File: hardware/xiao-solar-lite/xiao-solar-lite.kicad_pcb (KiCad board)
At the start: 2 copper layers, 30.5 x 28.5 mm, 36 parts, among them J1 SOLAR, J3 OUT (to Xiao 5V), J4 BATTERY, J5 I2C + CE, Q2 AO3400A (ship FET), U1 BQ25798RQMR

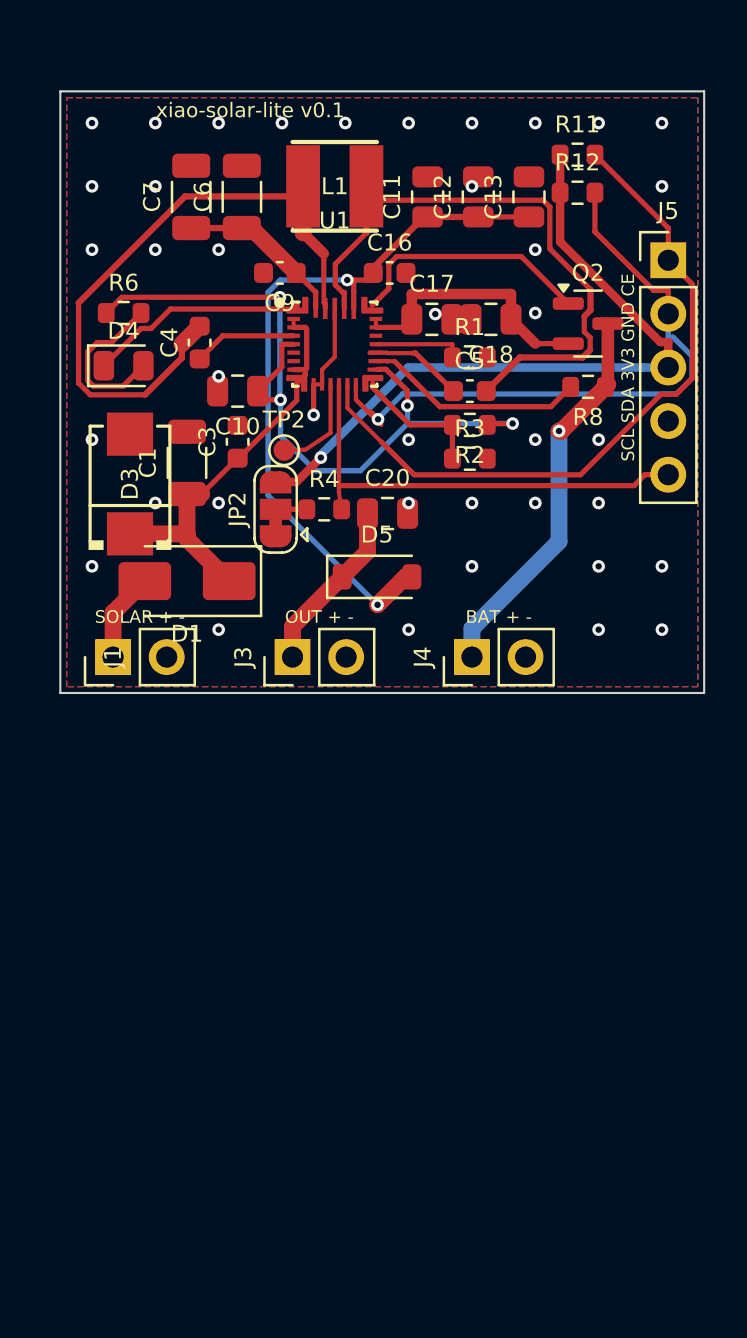
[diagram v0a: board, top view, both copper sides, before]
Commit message: hardware: xiao-solar-lite v0.2 as third layer under XIAO + Wio
The module now stacks under the standard XIAO nRF52840 + Wio-SX1262
sandwich through the 14 XIAO holes: CE on D0, SCL/SDA on D6/D7, 3V3,
GND, and SYS through B5819W to the 5V pin. 23 x 53 mm, charger below the
stack, only flat parts under it. Separate 4-pin I2C header for sensors.
Keepouts keep signal tracks off the L1 switch node and off the edge.

Co-Authored-By: Claude Opus 5.5 <noreply@anthropic.com>
Claude-Session: https://claude.ai/code/session_01P5Km81NY9NPL6RpKFGVEbH
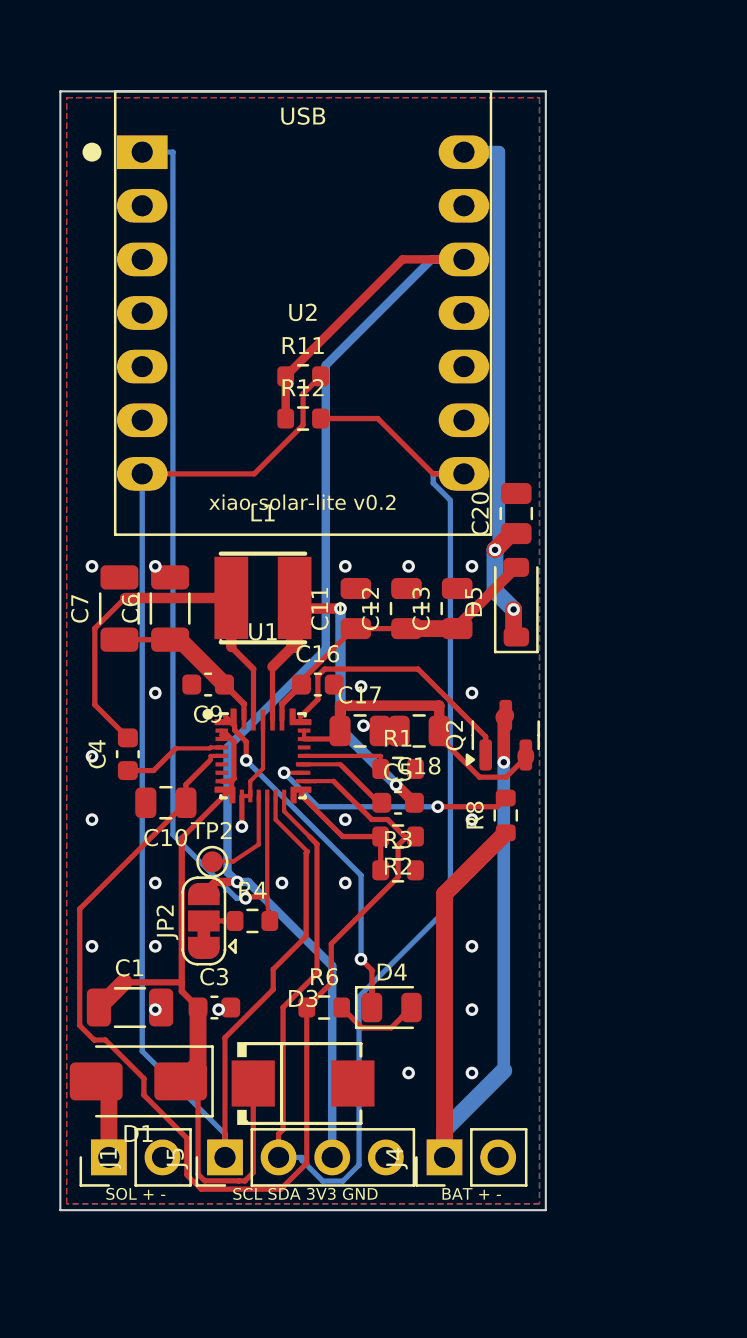
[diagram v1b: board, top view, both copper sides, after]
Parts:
- removed J3: OUT (to Xiao 5V), Connector_PinHeader_2.54mm:PinHeader_1x02_P2.54mm_Vertical
- added U2: XIAO + Wio stack, xiao_solar:XIAO_14P_2.54_21x17.8mm, F.Cu at (111.5, 110.5)
- J5: value I2C + CE -> I2C sensors; footprint Connector_PinHeader_2.54mm:PinHeader_1x05_P2.54mm_Vertical -> Connector_PinHeader_2.54mm:PinHeader_1x04_P2.54mm_Vertical
- moved J5 47.4 mm to (107.8, 150.5), turned to 90 degrees
- moved R6 34.2 mm to (112.5, 143.4)
- moved D4 32.9 mm to (115.7, 143.4)
- moved D3 29.6 mm to (111.5, 147.0), turned to 0 degrees
- moved C3 26.8 mm to (107.3, 143.4), turned to 0 degrees
- moved C1 25.9 mm to (103.3, 143.4), turned to 0 degrees
- moved D1 23.8 mm to (103.7, 146.9)
- moved J4 23.7 mm to (118.2, 150.5)
- moved J1 23.7 mm to (102.3, 150.5)
- moved R8 20.7 mm to (121.1, 134.3), turned to 90 degrees
- moved Q2 19.9 mm to (121.1, 130.5), turned to 90 degrees
- moved C17 19.8 mm to (114.2, 130.3)
- moved C18 19.8 mm to (117.0, 130.3)
- moved JP2 19.8 mm to (106.8, 139.3)
- moved R2 19.8 mm to (116.0, 135.3)
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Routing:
- net SDA: track 31.6 -> 67.4 mm, vias 1 -> 0
- net 3V3: track 33.3 -> 65.0 mm
- net SCL: track 33.2 -> 64.6 mm
- net BATT+: track 18.5 -> 38.8 mm
- net SYS: track 34.5 -> 14.7 mm, vias 2 -> 0
- net REGN: track 37.0 -> 55.7 mm, vias 4 -> 0
- net CE: track 26.9 -> 45.5 mm, vias 0 -> 1
- net VOUT: track 8.27 -> 26.4 mm, vias 0 -> 2
- net VBUS: track 19.9 -> 36.1 mm
- net SW1: track 30.4 -> 19.1 mm
- net SW2: track 29.1 -> 19.1 mm, vias 0 -> 2
- net STAT: track 10.4 -> 17.5 mm, vias 0 -> 2
- net LED_STAT: track 7.79 -> 4.79 mm
- net BAT: track 12.8 -> 15.3 mm
- net BATP: track 10.5 -> 12.3 mm, vias 0 -> 2
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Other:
- board size 30.5 x 28.5 mm -> 23 x 53 mm
- board text added: "SCL SDA 3V3 GND"
- board text added: "SOL + -"
- board text added: "xiao-solar-lite v0.2"
- board text removed: "OUT + -"
- board text removed: "SCL SDA 3V3 GND CE"
- board text removed: "SOLAR + -"
- board text removed: "xiao-solar-lite v0.1"

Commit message: hardware: charger zone per BQ25798 layout guide, v0.3 of both boards
- tools/charger.py: shared BQ25798 cluster (placement, PMID/SYS/VBUS/BAT/SW
  copper zones, hand routes) for xiao-solar and xiao-solar-lite
- 100 nF PMID/SYS caps at the pins, SW short and wide to L1, BTST/REGN/GND
  through vias under the package, BAT halves joined on B.Cu
- lite: TI cap counts (VBUS 2, PMID 3, SYS 5), 23 x 57 mm, D5 fed from SYS
- thermal spokes on small parts, solid on charger power caps
- routing: zone copper goes to Freerouting as fixed hatched wires, locked
  hand routes survive the finish pass; JLC CPL rotation fix for SOT-23/LED
- both boards 0 unconnected; READMEs, Gerber, BOM, CPL, PDFs, images

Co-Authored-By: Claude Opus 5.5 <noreply@anthropic.com>
Claude-Session: https://claude.ai/code/session_01P5Km81NY9NPL6RpKFGVEbH
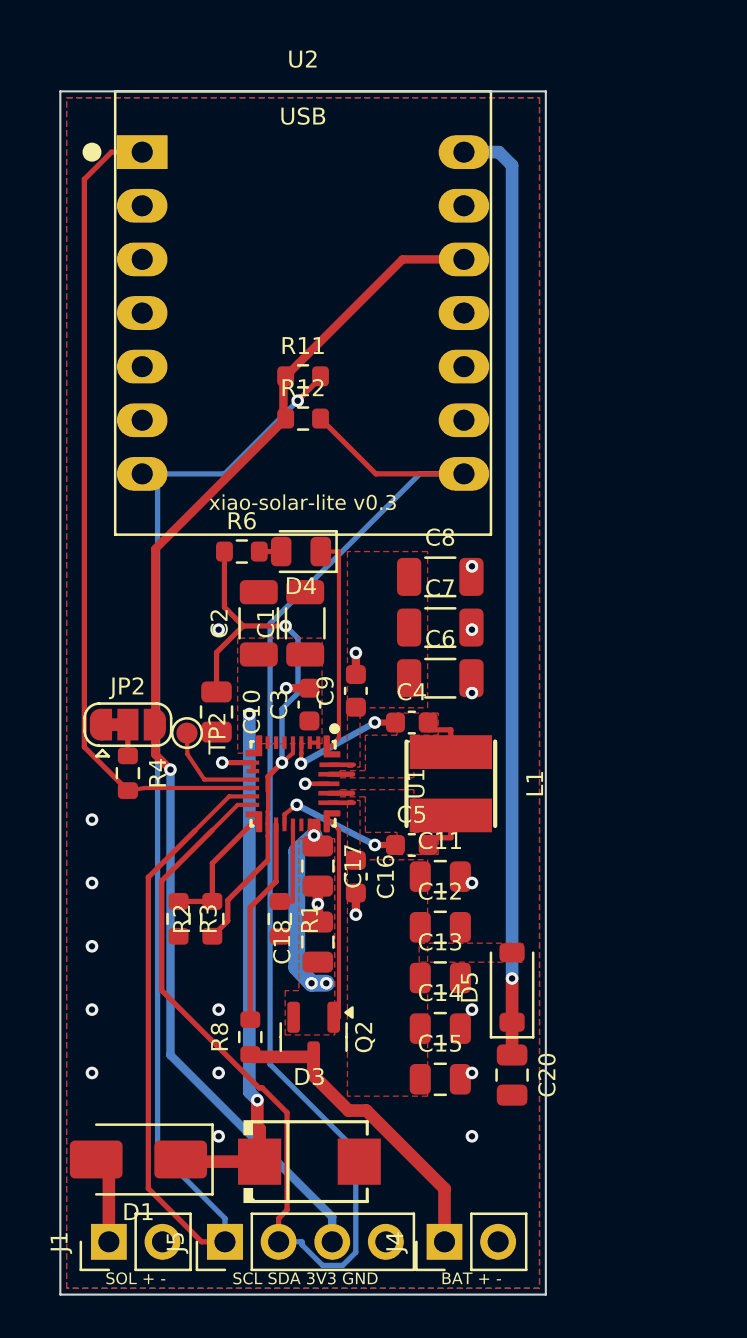
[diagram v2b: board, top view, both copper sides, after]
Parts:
- added C14: 10u/25V, Capacitor_SMD:C_0805_2012Metric, F.Cu at (118.0, 144.4)
- added C15: 10u/25V, Capacitor_SMD:C_0805_2012Metric, F.Cu at (118.0, 146.8)
- added C2: 10u/50V, Capacitor_SMD:C_1206_3216Metric, F.Cu at (109.4, 125.2)
- added C8: 10u/50V, Capacitor_SMD:C_1206_3216Metric, F.Cu at (118.0, 123.0)
- moved C20 26.6 mm to (121.4, 146.6), turned to -90 degrees
- moved D4 22.0 mm to (111.4, 121.8), turned to 180 degrees
- moved R6 21.9 mm to (108.6, 121.8)
- moved C1 20.0 mm to (111.6, 125.2), turned to 90 degrees
- moved D5 18.3 mm to (121.4, 142.4)
- moved C13 17.5 mm to (118.0, 142.0), turned to 0 degrees
- moved Q2 16.9 mm to (112.0, 144.8), turned to -90 degrees
- moved R8 16.0 mm to (109.0, 144.8)
- moved C7 15.2 mm to (118.0, 125.4), turned to 0 degrees
- moved C12 15.2 mm to (118.0, 139.6), turned to 0 degrees
- moved C3 15.0 mm to (111.8, 129.1), turned to 90 degrees
- moved C4 13.5 mm to (116.7, 129.9), turned to 0 degrees
- moved C11 13.3 mm to (118.0, 137.2), turned to 0 degrees
- moved C6 13.2 mm to (118.0, 127.8), turned to 0 degrees
- moved L1 12.5 mm to (118.5, 132.8), turned to -90 degrees
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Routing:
- net REGN: track 55.7 -> 27.4 mm, vias 0 -> 2
- net BATT+: track 38.8 -> 15.3 mm, vias 1 -> 0
- net VOUT: track 26.4 -> 44.7 mm, vias 2 -> 1
- net SW1: track 19.1 -> 3.62 mm
- net SW2: track 19.1 -> 3.62 mm, vias 2 -> 0
- net SDA: track 67.4 -> 81.5 mm
- net SYS: track 14.7 -> 1.18 mm
- net VBUS: track 36.1 -> 25.6 mm, vias 0 -> 2
- net SCL: track 64.6 -> 74.1 mm, vias 0 -> 1
- net STAT: track 17.5 -> 10.2 mm, vias 2 -> 0
- net 3V3: track 65.0 -> 57.9 mm
- net PMID: track 7.89 -> 1.15 mm
- net CE: track 45.5 -> 39.0 mm, vias 1 -> 0
- net BAT: track 15.3 -> 9.74 mm, vias 0 -> 3
- net LED_STAT: track 4.79 -> 1.04 mm
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- added copper zone on F.Cu, net BAT
- added copper zone on F.Cu, net PMID
- added copper zone on F.Cu, net SW1
- added copper zone on F.Cu, net SW2
- added copper zone on F.Cu, net SYS
- added copper zone on F.Cu, net VBUS
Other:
- board size 23 x 53 mm -> 23 x 57 mm
- board text added: "xiao-solar-lite v0.3"
- board text removed: "xiao-solar-lite v0.2"

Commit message: hardware: two vias per power layer change, no vias in pads
- BAT halves joined on B.Cu with two vias at each end (C17/C18/Q2 moved)
- refill.py: second via next to every power-net via that is alone
- lite: VBUS from the input diodes as one 0.8 mm B.Cu run, two vias at
  each end; main: fixed landing vias for the VBUS bus in the VBUS copper
- stitching/island vias stay off pads (kicad-happy VP-001 findings)
- main: own GND via for C22 between the module rows
- Gerber, BOM, CPL, PDFs and images regenerated; both boards 0 unconnected

Co-Authored-By: Claude Opus 5.5 <noreply@anthropic.com>
Claude-Session: https://claude.ai/code/session_01P5Km81NY9NPL6RpKFGVEbH
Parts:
- moved C17 1.60 mm to (112.2, 138.3)
- moved C18 1.60 mm to (112.2, 141.9)
- moved Q2 1.60 mm to (112.0, 146.4)
- moved R8 1.60 mm to (109.0, 146.4)
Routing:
- net SCL: track 74.1 -> 51.5 mm, vias 1 -> 2
- net VBUS: track 25.6 -> 35.9 mm, vias 2 -> 6
- net SDA: track 81.5 -> 76.1 mm
- net 3V3: track 57.9 -> 63.4 mm
- net REGN: track 27.4 -> 23.2 mm
- net BAT: track 9.74 -> 12.6 mm, vias 3 -> 4
- net VOUT: track 44.7 -> 46.7 mm, vias 1 -> 2
- net BATT+: track 15.3 -> 13.7 mm
- net SDRV: track 9.65 -> 11.2 mm
- net BATP: track 9.76 -> 11.4 mm
- net GND: vias 22 -> 12

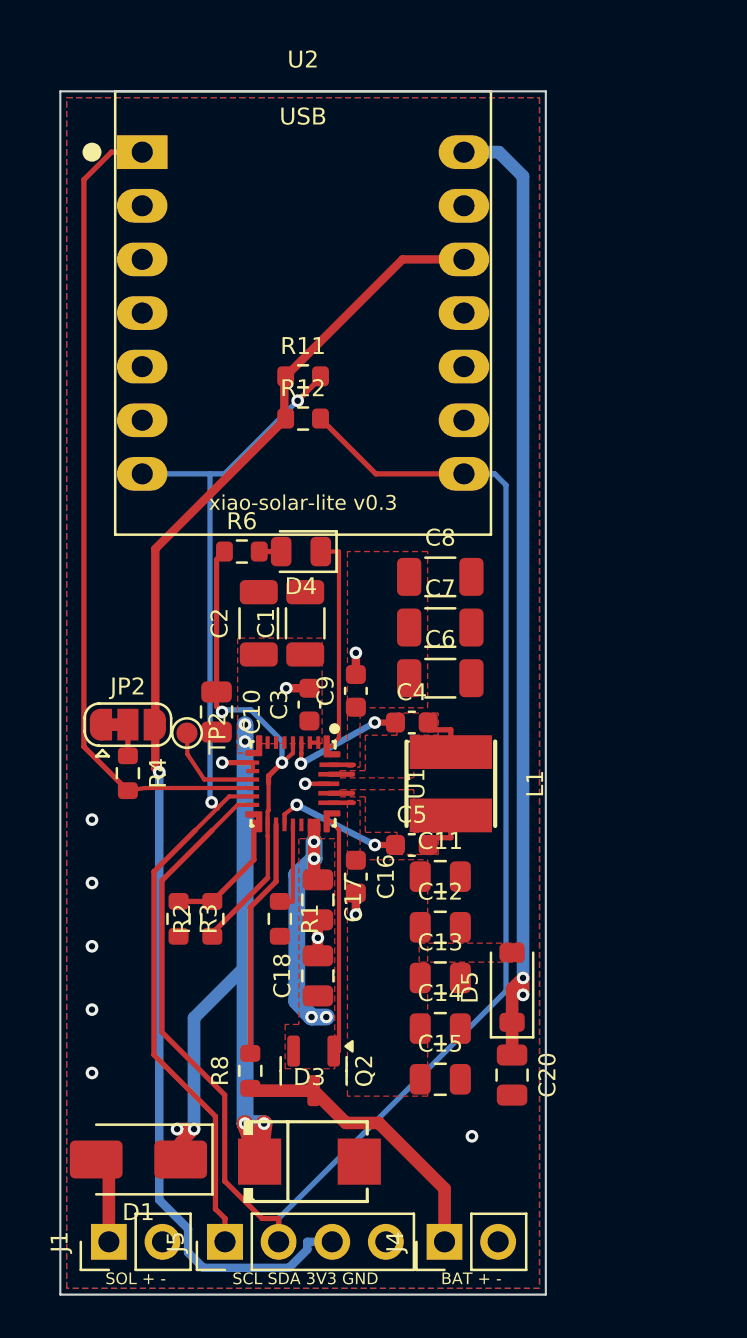
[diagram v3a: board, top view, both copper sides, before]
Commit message: hardware: xiao-solar v0.4 (no loads, INA219, 48x71.5) + block schematics for both boards
Co-Authored-By: Claude Opus 5.5 <noreply@anthropic.com>
Claude-Session: https://claude.ai/code/session_01P5Km81NY9NPL6RpKFGVEbH
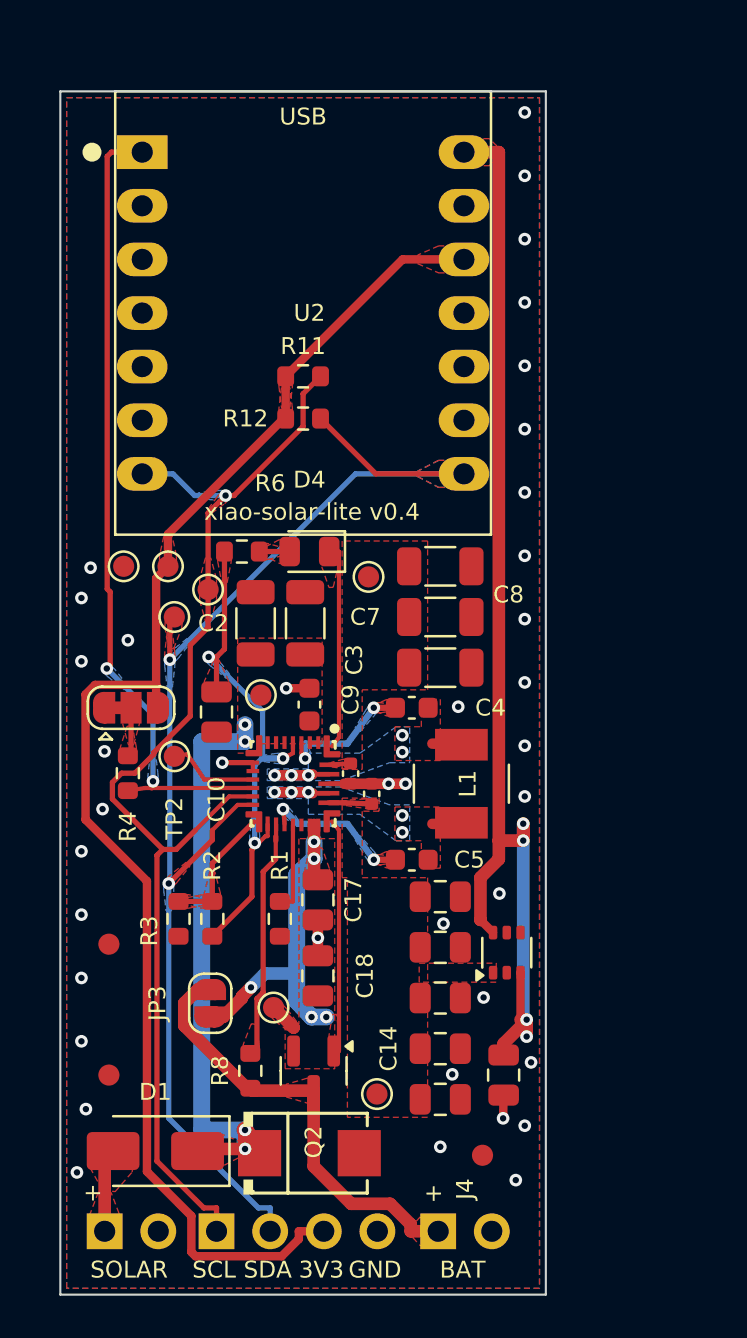
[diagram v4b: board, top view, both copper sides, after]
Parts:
- added FID1: Fiducial, Fiducial_1mm_Mask2mm, F.Cu at (102.3, 140.4)
- added FID2: Fiducial, Fiducial_1mm_Mask2mm, F.Cu at (120.0, 150.4)
- added FID3: Fiducial, Fiducial_1mm_Mask2mm, F.Cu at (102.3, 146.6)
- added JP3: no ship FET (LiFePO4), Jumper:SolderJumper-2_P1.3mm_Open_RoundedPad1.0x1.5mm, F.Cu at (107.1, 143.2)
- added TP10: SDA, TestPoint:TestPoint_Pad_D1.0mm, F.Cu at (105.4, 124.9)
- added TP3: VBUS, TestPoint:TestPoint_Pad_D1.0mm, F.Cu at (109.5, 128.6)
- added TP4: PMID, TestPoint:TestPoint_Pad_D1.0mm, F.Cu at (114.6, 123.0)
- added TP5: SYS, TestPoint:TestPoint_Pad_D1.0mm, F.Cu at (115.0, 147.5)
- added TP6: BAT, TestPoint:TestPoint_Pad_D1.0mm, F.Cu at (110.1, 143.4)
- added TP7: GND, TestPoint:TestPoint_Pad_D1.0mm, F.Cu at (103.0, 122.5)
- added TP8: 3V3, TestPoint:TestPoint_Pad_D1.0mm, F.Cu at (105.1, 122.5)
- added TP9: SCL, TestPoint:TestPoint_Pad_D1.0mm, F.Cu at (107.0, 123.6)
- C16: footprint Capacitor_SMD:C_0603_1608Metric -> Capacitor_SMD:C_0402_1005Metric
- C9: value 100n -> 100n/50V; footprint Capacitor_SMD:C_0603_1608Metric -> Capacitor_SMD:C_0402_1005Metric
- D1: value SS34 -> SS54
- D5: value B5819W -> LM66100; footprint Diode_SMD:D_SOD-123 -> Package_TO_SOT_SMD:SOT-363_SC-70-6
- L1: value 2.2uH 3.2A -> 2.2uH 4A molded (MWSA0402S); footprint xiao_solar:IND-SMD_L4.0-W4.0_FNR40XXS -> xiao_solar:IND-SMD_L4.4-W4.2_MWSA0402S
- moved C16 3.99 mm to (114.8, 133.3), turned to 90 degrees
- moved C9 3.93 mm to (113.8, 132.3), turned to -90 degrees
- moved D5 1.67 mm to (121.2, 140.8)
- moved TP2 1.25 mm to (105.4, 131.5)
- moved C11 0.95 mm to (118.0, 138.2)
- moved C12 0.95 mm to (118.0, 140.6)
- moved C13 0.95 mm to (118.0, 142.9)
- moved C14 0.95 mm to (118.0, 145.3)
- moved C15 0.95 mm to (118.0, 147.8)
- moved D1 0.89 mm to (104.5, 150.2)
- moved JP2 0.81 mm to (103.3, 129.2)
- moved C4 0.70 mm to (116.7, 129.2)
- moved C5 0.70 mm to (116.7, 136.4)
- moved J5 0.64 mm to (107.4, 154.0)
- moved J4 0.58 mm to (117.9, 154.0)
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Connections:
- D5 pad 1: VOUT -> SYS
- D5 pad 2: SYS -> GND
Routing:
- net SDA: track 76.1 -> 62.8 mm, vias 0 -> 2
- net VOUT: track 46.7 -> 57.5 mm, vias 2 -> 4
- net BATT+: track 13.7 -> 21.8 mm
- net VBUS: track 35.9 -> 28.9 mm, vias 6 -> 4
- net BAT: track 12.6 -> 19.0 mm, vias 4 -> 5
- net SCL: track 51.5 -> 57.5 mm, vias 2 -> 1
- net 3V3: track 63.4 -> 68.2 mm, vias 1 -> 0
- net REGN: track 23.2 -> 25.8 mm, vias 2 -> 3
- net GND: track 7.82 -> 9.38 mm, vias 12 -> 39
- net CE_PULL: track 1.47 -> 2.34 mm
- net BTST2: track 6.33 -> 7.19 mm
- net SYS: track 1.18 -> 2.03 mm
- net BTST1: track 5.98 -> 6.64 mm
- net CE: track 39.0 -> 38.7 mm, vias 0 -> 2
- net SW2: track 3.62 -> 3.97 mm, vias 0 -> 5
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- added copper zone on F.Cu, net 3V3
- added copper zone on F.Cu, net BATP
- added copper zone on F.Cu, net BATT+
- added copper zone on B.Cu, net BTST1
- added copper zone on F.Cu, net BTST1
- added copper zone on B.Cu, net BTST2
- added copper zone on F.Cu, net BTST2
- added copper zone on B.Cu, net CE
- added copper zone on F.Cu, net CE_PULL
- added copper zone on F.Cu, net LED_STAT
- added copper zone on B.Cu, net REGN
- added copper zone on F.Cu, net REGN
- added copper zone on B.Cu, net SCL
- added copper zone on F.Cu, net SCL
- added copper zone on B.Cu, net SDA
- added copper zone on F.Cu, net SDA
- added copper zone on F.Cu, net SDRV
- added copper zone on F.Cu, net SOLAR_IN
- added copper zone on F.Cu, net STAT
- added copper zone on B.Cu, net SW1
- added copper zone on B.Cu, net SW2
- added copper zone on F.Cu, net TS
- added copper zone on F.Cu, net VOUT
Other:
- board text added: "+"
- board text added: "3V3"
- board text added: "BAT"
- board text added: "GND"
- board text added: "SCL"
- board text added: "SDA"
- board text added: "SOLAR"
- board text added: "xiao-solar-lite v0.4"
- board text removed: "BAT + -"
- board text removed: "SCL SDA 3V3 GND"
- board text removed: "SOL + -"
- board text removed: "xiao-solar-lite v0.3"
